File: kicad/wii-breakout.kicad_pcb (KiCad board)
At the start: 2 copper layers, 64.5 x 8.5 mm, 12 parts, among them J1 Peripherals, J10 ⏚, J2 Audio, J3 Video, J4 USB, J5 GC, J6 Reset, J7 BT, J8 Audio, J9 Video

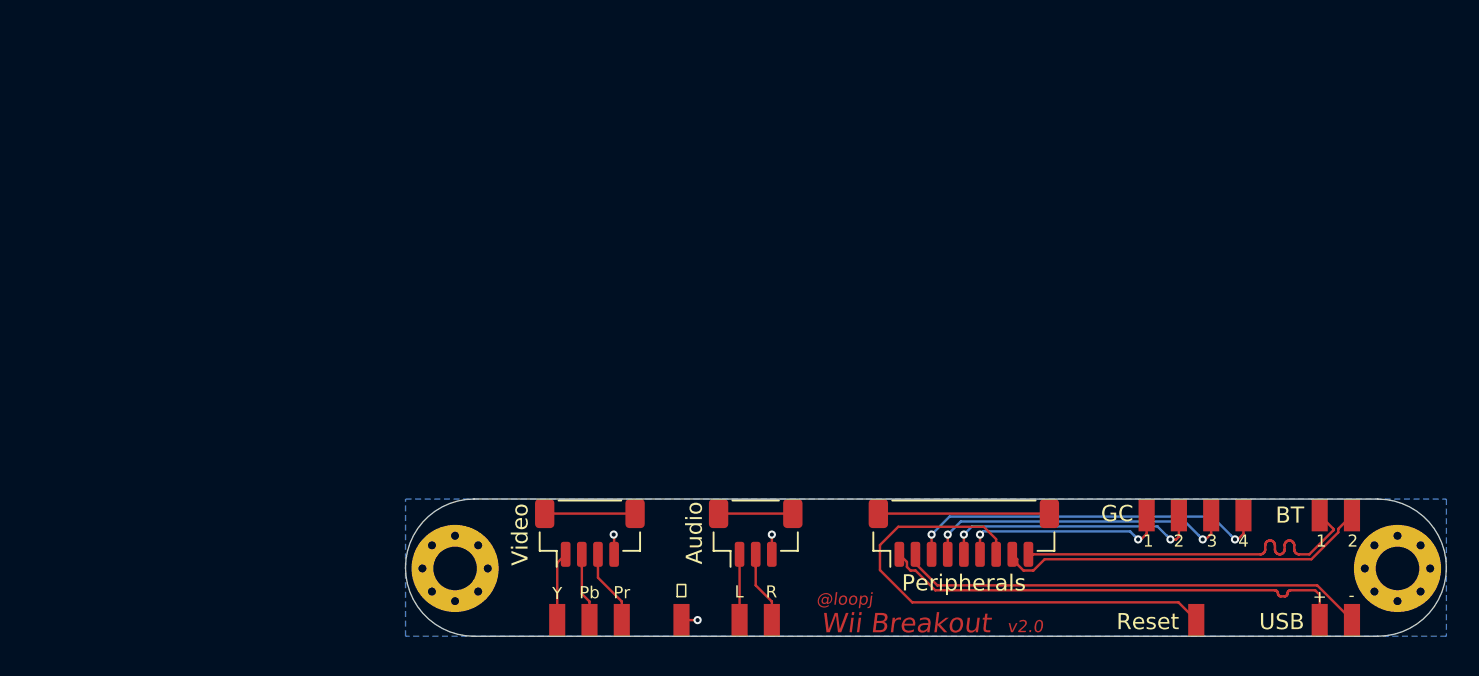
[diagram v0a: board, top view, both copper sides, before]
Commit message: v3.0 - minimal size, cutout for mobo cap, split USB from data header, reorder GC lines to match mobo
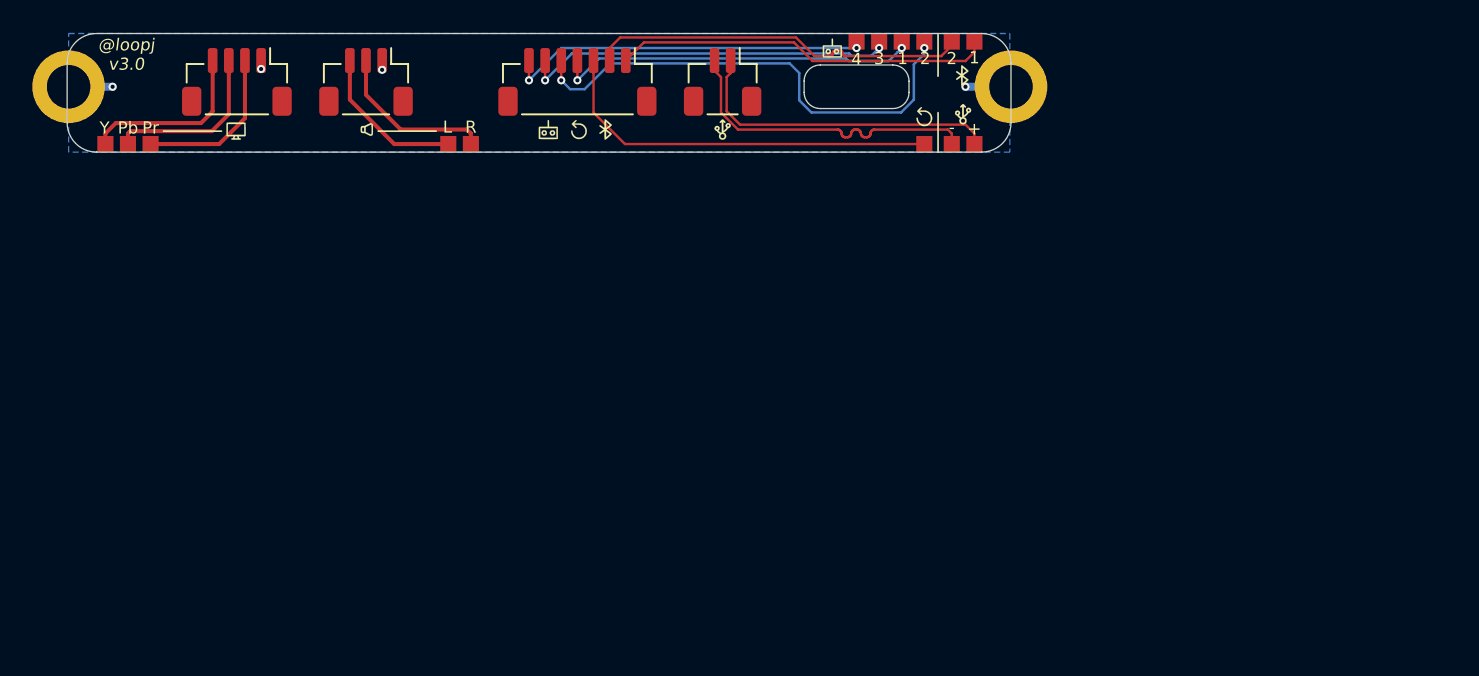
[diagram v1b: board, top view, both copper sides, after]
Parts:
- added ?: LOGO, project-footprints:usb, F.Cu at (51.5, 77.2)
- added G***: LOGO, project-footprints:controller, F.Cu at (58.4, 72.2)
- added G***: LOGO, project-footprints:controller, F.Cu at (40.8, 77.2)
- added G***: LOGO, project-footprints:bluetooth, F.Cu at (44.3, 77.2)
- added G***: LOGO, project-footprints:reset, F.Cu at (42.6, 77.2)
- added G***: LOGO, project-footprints:reset, F.Cu at (64.0, 76.4)
- added G***: LOGO, project-footprints:bluetooth, F.Cu at (66.4, 73.8)
- added G***: LOGO, project-footprints:usb, F.Cu at (66.5, 76.2)
- added G***: LOGO, project-footprints:audio, F.Cu at (29.5, 77.2)
- added G***: LOGO, project-footprints:video, F.Cu at (21.4, 77.3)
- H1, H2: footprint MountingHole:MountingHole_2.7mm_M2.5_Pad_Via -> MountingHole:MountingHole_2.7mm_M2.5_ISO14580_Pad
- J1: footprint Connector_JST:JST_SH_BM09B-SRSS-TB_1x09-1MP_P1.00mm_Vertical -> Connector_JST:JST_SH_BM07B-SRSS-TB_1x07-1MP_P1.00mm_Vertical
- J10: value ⏚ -> USB; footprint project-footprints:TestPoint_Pad_2.0x1.0mm -> Connector_JST:JST_SH_BM02B-SRSS-TB_1x02-1MP_P1.00mm_Vertical
- J6: value Reset -> RST
- moved J9 41.1 mm to (14.7, 78.1)
- moved H1 38.3 mm to (69.4, 74.5)
- moved H2 38.3 mm to (11.0, 74.5)
- moved J4 37.5 mm to (66.5, 78.1)
- moved J7 37.4 mm to (66.5, 71.8)
- moved J2 36.9 mm to (29.4, 74.2), turned to 180 degrees
- moved J1 36.8 mm to (42.5, 74.2), turned to 180 degrees
- moved J3 35.5 mm to (21.4, 74.2), turned to 180 degrees
- moved J5 34.9 mm to (62.0, 71.8)
- moved J8 34.7 mm to (35.2, 78.1)
- moved J6 34.0 mm to (64.0, 78.1)
- moved J10 33.4 mm to (51.5, 74.2), turned to 180 degrees
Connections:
- J1 pad 1: /USB_D+ -> /BT_D-
- J1 pad 2: /USB_D- -> /BT_D+
- J1 pad 3: /GC_4 -> /RST
- J1 pad 4: /GC_3 -> /GC_1
- J1 pad 6: /GC_1 -> /GC_3
- J1 pad 7: /RST -> /GC_4
- J1 pad MP: Net-(J1-PadMP) -> (no net)
- J10 pad 1: GND -> /USB_D+
- J2 pad 1: /AUDIO_LEFT -> GND
- J2 pad 3: GND -> /AUDIO_LEFT
- J2 pad MP: Net-(J2-PadMP) -> (no net)
- J3 pad 1: /VIDEO_Y -> GND
- J3 pad 2: /VIDEO_PB -> /VIDEO_PR
- J3 pad 3: /VIDEO_PR -> /VIDEO_PB
- J3 pad 4: GND -> /VIDEO_Y
- J3 pad MP: Net-(J3-PadMP) -> (no net)
- J4 pad 1: /USB_D+ -> /USB_D-
- J4 pad 2: /USB_D- -> /USB_D+
- J5 pad 1: /GC_4 -> /GC_2
- J5 pad 2: /GC_3 -> /GC_1
- J5 pad 3: /GC_2 -> /GC_3
- J5 pad 4: /GC_1 -> /GC_4
- J7 pad 1: /BT_D+ -> /BT_D-
- J7 pad 2: /BT_D- -> /BT_D+
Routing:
- net /GC_2: track 16.5 -> 30.0 mm
- net Net-(J1-PadMP): track 10.6 -> 0.00 mm
- net /USB_D+: track 29.3 -> 19.8 mm
- net /GC_1: track 13.1 -> 22.3 mm
- net /USB_D-: track 29.1 -> 20.0 mm
- net /RST: track 31.4 -> 24.5 mm
- net /VIDEO_Y: track 4.29 -> 11.0 mm
- net /VIDEO_PB: track 4.27 -> 10.7 mm
- net /AUDIO_RIGHT: track 4.49 -> 10.3 mm
- net Net-(J3-PadMP): track 5.60 -> 0.00 mm
- net /AUDIO_LEFT: track 4.07 -> 9.66 mm
- net /VIDEO_PR: track 4.69 -> 10.1 mm
- net Net-(J2-PadMP): track 4.60 -> 0.00 mm
- net /GC_3: track 19.6 -> 22.9 mm
- net GND: track 3.46 -> 5.85 mm, vias 3 -> 4
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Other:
- board size 64.5 x 8.5 mm -> 58.5 x 7.4 mm
- board text added: "v3.0"
- board text removed: "Wii Breakout"
- board text removed: "v2.0"
